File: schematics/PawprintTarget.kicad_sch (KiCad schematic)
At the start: 60 parts, among them J1 Conn_01x15, J2 Conn_01x15, J4 RJ45, J5 RJ45, J8 Motor, J9 Motor, Q1 2N7002BK, Q2 2N7002BK, SW1 SW_DIP_x04, SW2 SW_DIP_x04, U1 MAX485E, U2 EAIRMCA1, U3 Mini360

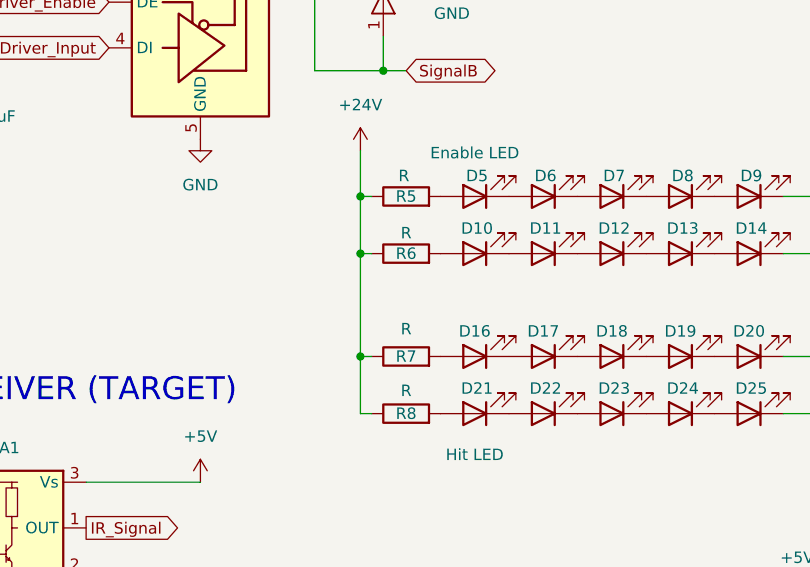
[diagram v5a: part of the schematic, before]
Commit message: Add interactive BOM
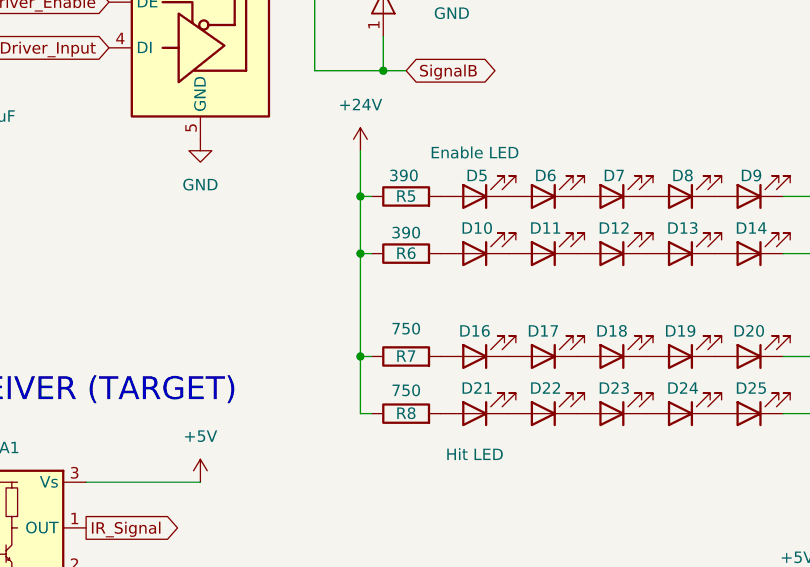
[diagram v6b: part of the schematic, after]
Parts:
- R5, R6: value R -> 390
- R7, R8: value R -> 750
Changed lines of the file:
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@@
 			)
 		)
-		(property "Value" "R"
+		(property "Value" "390"
 			(at 203.2 63.754 90)
 			(effects
@@
 			)
 		)
-		(property "Value" "R"
+		(property "Value" "750"
 			(at 203.2 81.28 90)
 			(effects
@@
 			)
 		)
-		(property "Value" "R"
+		(property "Value" "750"
 			(at 203.2 74.422 90)
 			(effects
@@
 			)
 		)
-		(property "Value" "R"
+		(property "Value" "390"
 			(at 202.946 57.404 90)
 			(effects
